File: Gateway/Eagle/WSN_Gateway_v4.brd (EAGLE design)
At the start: 98.7 x 27.9 mm, 15 parts, among them J1 5.5x2.1mm Barrel

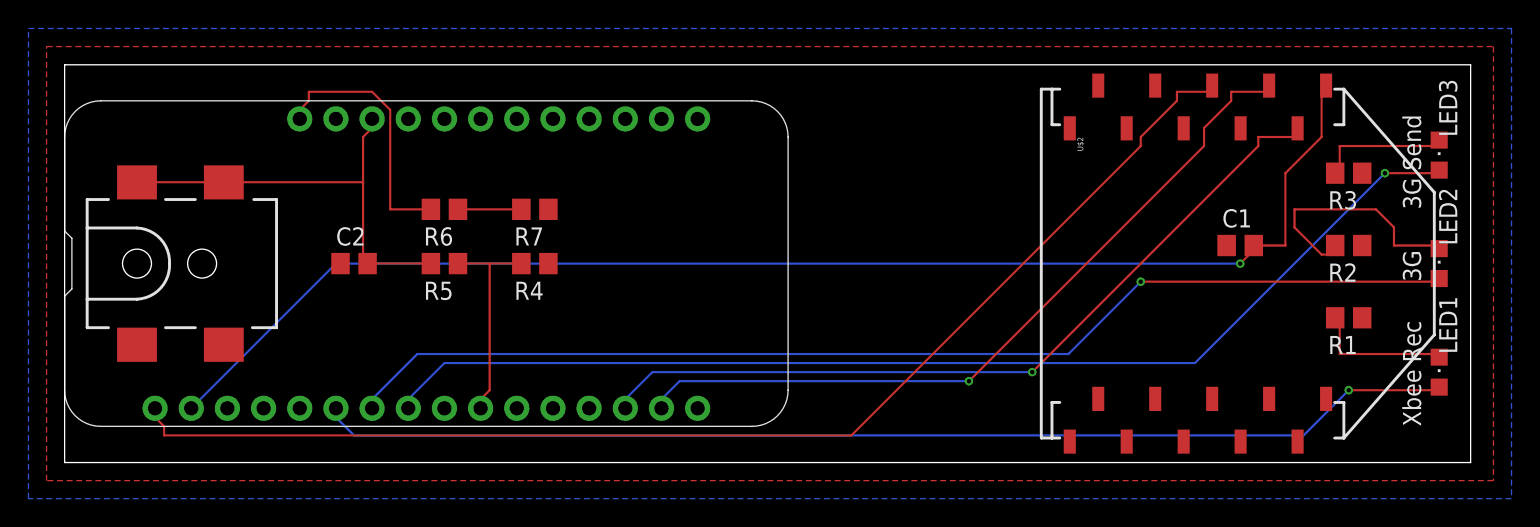
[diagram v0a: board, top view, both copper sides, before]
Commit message: Added SMD pin headers to gateway board
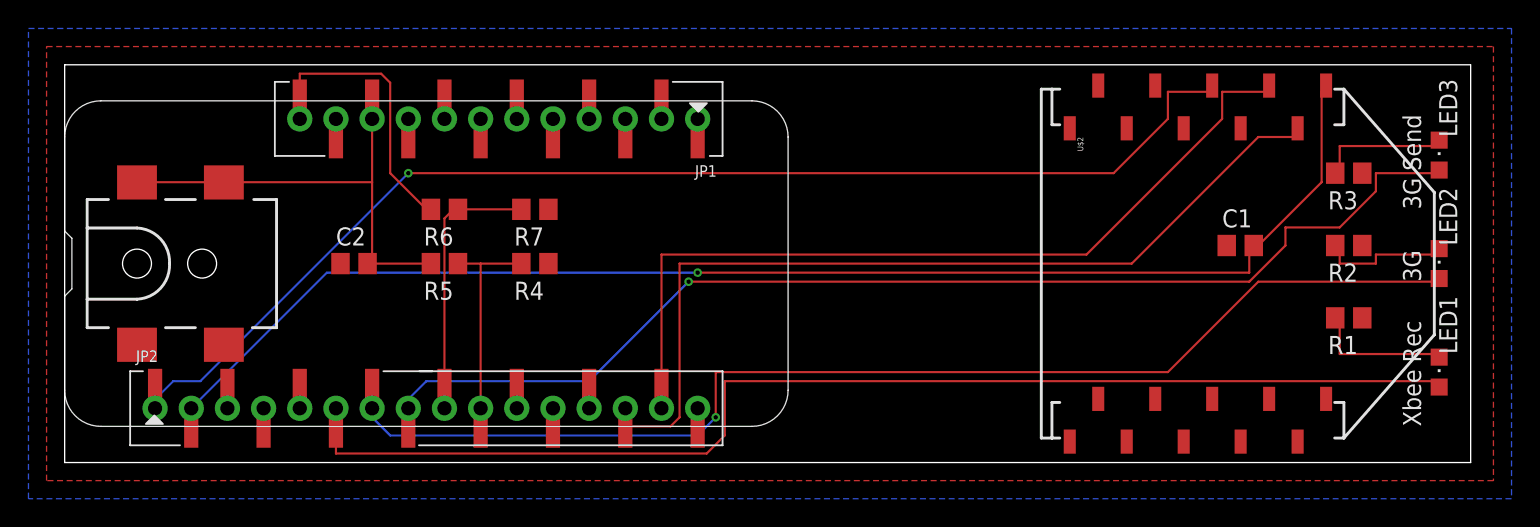
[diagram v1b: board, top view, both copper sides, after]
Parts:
- added JP1: (no value), pinhead+:1X12_SMT
- added JP2: (no value), pinhead+:1X16_SMT
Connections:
- removed net VBAT_MEAS: MS1.9
- new net N$19: JP1.1
- new net N$21: JP1.2
- new net N$22: JP1.3
- new net N$23: JP1.4
- new net N$24: JP1.5
- new net N$25: JP1.6
- new net N$26: JP1.7
- new net N$27: JP1.8
- new net N$28: JP1.9
- new net N$29: U$2.6
- new net N$30: JP1.11
- new net N$31: U$2.4
- new net N$32: JP2.16
- new net N$33: U$2.7
- new net N$34: U$2.8
- new net N$35: JP2.13
- new net N$36: JP2.12
- new net N$37: JP2.11
- new net N$38: U$2.9
- new net N$39: U$2.20
- new net N$40: U$2.19
- new net N$41: U$2.18
- new net N$42: U$2.17
- new net N$43: JP2.5
- new net N$44: U$2.16
- new net N$45: JP2.3
- new net N$46: U$2.15
- new net N$47: U$2.14
- new net N$48: U$2.13
- new net N$49: U$2.11
- net 3V: now also JP2.2
- net GND: now also JP2.4
- net LED1: now also JP2.6
- net LED2: now also JP2.7
- net LED3: now also JP2.8
- net RESET: now also JP2.1
- net USB: now also JP1.10
- net USB_MEASURE: now also JP2.10
- net VBAT: now also JP1.12
- net VBAT_MEASURE: now also JP2.9, MS1.9
- net XBEE_RX: now also JP2.15
- net XBEE_TX: now also JP2.14
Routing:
- net VBAT_MEASURE: track 4.45 -> 19.0 mm
- net N$2: track 17.7 -> 9.62 mm
- net XBEE_TX: track 56.3 -> 63.9 mm, vias 1 -> 0
- net XBEE_RX: track 53.7 -> 59.6 mm, vias 1 -> 0
- net LED1: track 80.2 -> 85.4 mm, vias 1 -> 0
- net LED2: track 79.2 -> 84.2 mm
- net LED3: track 79.8 -> 82.8 mm
- net VBAT: track 18.3 -> 20.1 mm
- net USB: track 31.1 -> 32.7 mm
- net USB_MEASURE: track 14.9 -> 16.1 mm
- net 3V: track 94.3 -> 95.5 mm
- net RESET: track 87.0 -> 86.9 mm, vias 0 -> 1

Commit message: minor changes to gateway eagle files
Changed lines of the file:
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@@
 </polygon>
 <contactref element="JP2" pad="4"/>
-<wire x1="81.6" y1="15.24" x2="91.12" y2="15.24" width="0" layer="19" extent="1-1"/>
-<wire x1="70.58" y1="23.47" x2="81.6" y2="15.24" width="0" layer="19" extent="1-1"/>
-<wire x1="33.97" y1="17.78" x2="70.58" y2="23.47" width="0" layer="19" extent="1-1"/>
-<wire x1="19.37" y1="13.97" x2="33.97" y2="13.97" width="0" layer="19" extent="1-1"/>
+<via x="55.88" y="17.78" extent="1-16" drill="0.35"/>
+<via x="55.88" y="24.13" extent="1-16" drill="0.35"/>
+<via x="78.74" y="15.24" extent="1-16" drill="0.35"/>
+<via x="55.88" y="10.16" extent="1-16" drill="0.35"/>
+<via x="55.88" y="2.54" extent="1-16" drill="0.35"/>
 </signal>
 <signal name="3V">
@@
 </signal>
 </signals>
+<errors>
+</errors>
 </board>
 </drawing>
